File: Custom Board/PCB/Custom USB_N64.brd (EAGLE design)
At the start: 86 x 38.1 mm, 25 parts, among them J1 N64_Data, J2 N64_GND, U1 STM32F446RET6

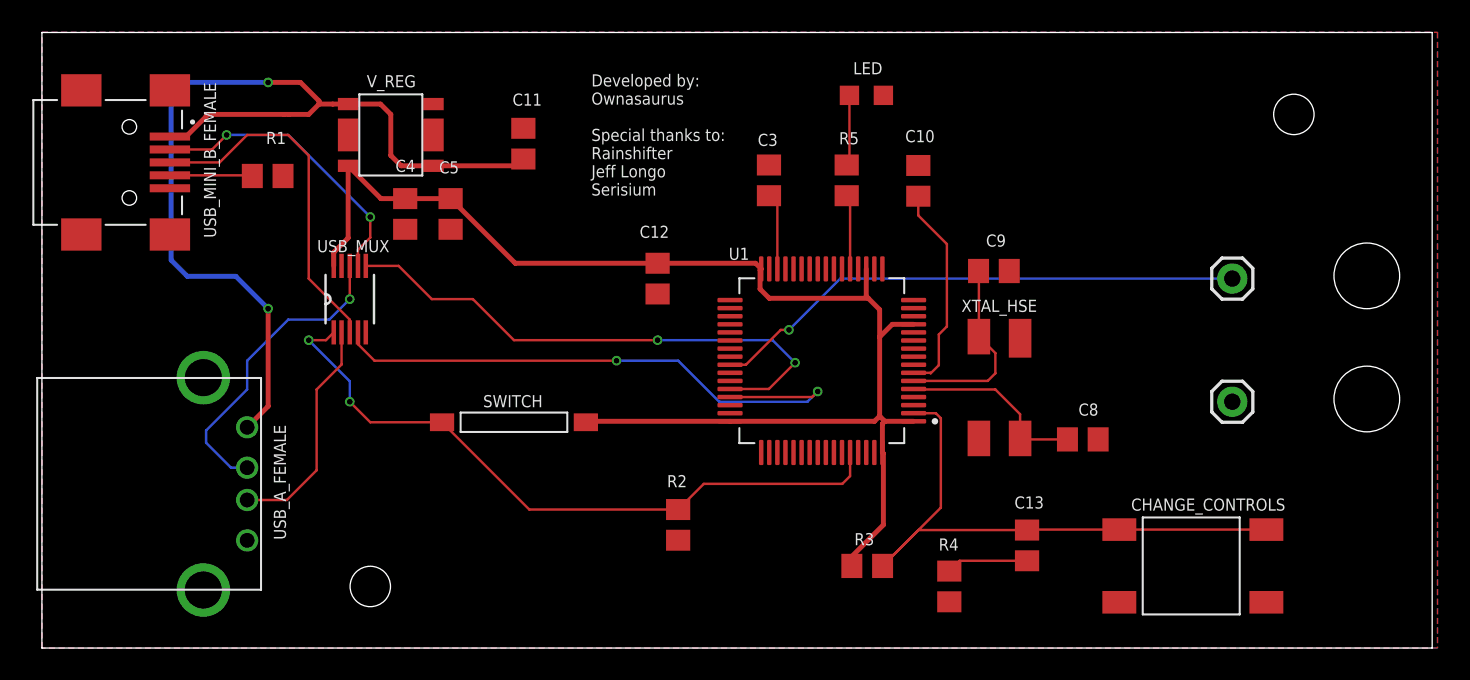
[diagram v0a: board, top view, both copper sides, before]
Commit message: fixed faulty V_REG foorprint and N64 silkscreen
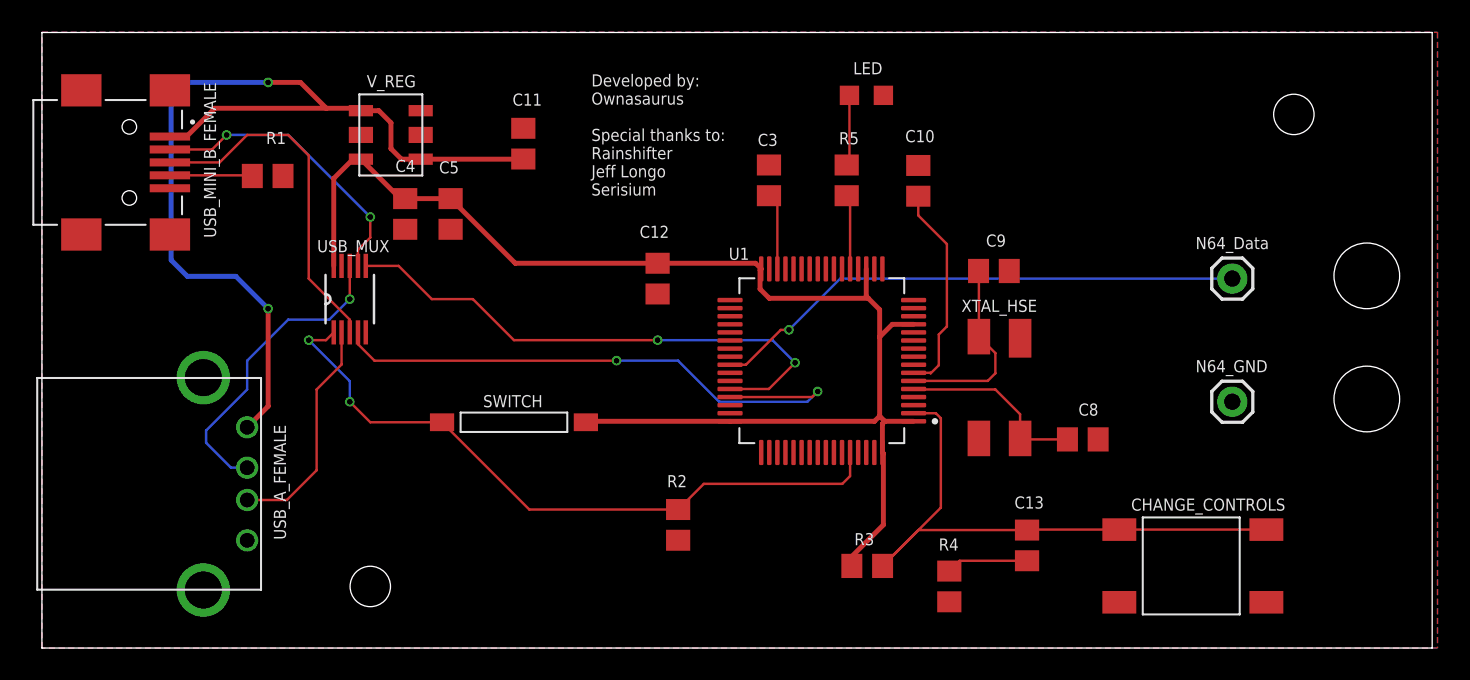
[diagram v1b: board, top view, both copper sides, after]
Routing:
- net +5V: track 61.3 -> 60.6 mm
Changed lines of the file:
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@@
 <drawing>
 <settings>
-<setting alwaysvectorfont="yes"/>
+<setting alwaysvectorfont="no"/>
 <setting verticaltext="up"/>
 </settings>
@@
 </element>
 <element name="J1" library="SparkFun-Connectors" package="1X01" value="N64_Data" x="73.66" y="22.86" smashed="yes">
-<attribute name="VALUE" x="71.39" y="24.685" size="0.75" layer="27" font="vector" ratio="15"/>
+<attribute name="VALUE" x="71.39" y="24.685" size="0.75" layer="25" font="vector" ratio="15"/>
 </element>
 <element name="J2" library="SparkFun-Connectors" package="1X01" value="N64_GND" x="73.66" y="15.24" smashed="yes">
-<attribute name="VALUE" x="71.39" y="17.065" size="0.75" layer="27" font="vector" ratio="15"/>
+<attribute name="VALUE" x="71.39" y="17.065" size="0.75" layer="25" font="vector" ratio="15"/>
 </element>
 <element name="C11" library="eagle-ltspice" library_urn="urn:adsk.eagle:library:217" package="C0805" package3d_urn="urn:adsk.eagle:package:13265/1" value="100nF" x="29.79" y="31.21" smashed="yes" rot="R270">
@@
 <wire x1="38.1" y1="23.81" x2="44.16" y2="23.81" width="0.3048" layer="1"/>
 <wire x1="44.51" y1="23.46" x2="44.16" y2="23.81" width="0.3048" layer="1"/>
-<wire x1="18.95" y1="29.84" x2="18.95" y2="25.37545" width="0.3048" layer="1"/>
 <wire x1="44.4382" y1="22.21375" x2="44.4382" y2="23.3882" width="0.3048" layer="1"/>
 <wire x1="53.94" y1="20.03" x2="52.62195" y2="20.03" width="0.3048" layer="1"/>
@@
 <wire x1="51.01" y1="21.76895" x2="51.01" y2="23.46" width="0.3048" layer="1"/>
 <wire x1="44.4382" y1="23.3882" x2="44.51" y2="23.46" width="0.3048" layer="1"/>
-<wire x1="18.95" y1="25.37545" x2="18.0594" y2="24.48485" width="0.3048" layer="1"/>
-<wire x1="18.0594" y1="24.48485" x2="18.0594" y2="23.6474" width="0.3048" layer="1"/>
 <wire x1="51.8392" y1="20.93975" x2="51.8392" y2="19.24725" width="0.3048" layer="1"/>
 <wire x1="51.8392" y1="14.351" x2="51.8392" y2="19.24725" width="0.3048" layer="1"/>
@@
 <wire x1="52.01" y1="12.1" x2="52.01" y2="13.8798" width="0.3048" layer="1"/>
 <wire x1="52.01" y1="13.8798" x2="52.1602" y2="14.03" width="0.3048" layer="1"/>
-<wire x1="18.95" y1="29.84" x2="20.98" y2="27.81" width="0.3048" layer="1"/>
-<wire x1="20.98" y1="27.81" x2="22.48" y2="27.81" width="0.3048" layer="1"/>
 <wire x1="22.48" y1="27.81" x2="25.29" y2="27.81" width="0.3048" layer="1"/>
 <wire x1="25.29" y1="27.81" x2="29.29" y2="23.81" width="0.3048" layer="1"/>
 <wire x1="29.29" y1="23.81" x2="38.1" y2="23.81" width="0.3048" layer="1"/>
+<wire x1="18.0594" y1="23.6474" x2="18.0594" y2="29.0594" width="0.3048" layer="1"/>
+<wire x1="19.25" y1="30.25" x2="19.74" y2="30.25" width="0.3048" layer="1"/>
+<wire x1="18.0594" y1="29.0594" x2="19.25" y2="30.25" width="0.3048" layer="1"/>
+<wire x1="19.74" y1="30.25" x2="22.18" y2="27.81" width="0.3048" layer="1"/>
+<wire x1="22.18" y1="27.81" x2="22.48" y2="27.81" width="0.3048" layer="1"/>
 </signal>
 <signal name="N$5">
@@
 <contactref element="V_REG" pad="EN"/>
 <contactref element="USB_MINI_B_FEMALE" pad="1"/>
-<wire x1="8.92" y1="31.65" x2="10.135" y2="32.865" width="0.3048" layer="1"/>
-<wire x1="10.29" y1="33.02" x2="10.135" y2="32.865" width="0.3048" layer="1"/>
-<wire x1="17.15" y1="33.66" x2="16.51" y2="33.02" width="0.3048" layer="1"/>
-<wire x1="17.15" y1="33.66" x2="18" y2="33.66" width="0.3048" layer="1"/>
-<wire x1="18" y1="33.66" x2="18.95" y2="33.66" width="0.3048" layer="1"/>
-<wire x1="18.95" y1="33.66" x2="20.95" y2="33.66" width="0.3048" layer="1"/>
-<wire x1="20.95" y1="33.66" x2="21.59" y2="33.02" width="0.3048" layer="1"/>
-<wire x1="21.59" y1="33.02" x2="21.59" y2="30.48" width="0.3048" layer="1"/>
-<wire x1="21.59" y1="30.48" x2="22.23" y2="29.84" width="0.3048" layer="1"/>
-<wire x1="22.23" y1="29.84" x2="24.23" y2="29.84" width="0.3048" layer="1"/>
 <contactref element="USB_A_FEMALE" pad="+5V"/>
 <wire x1="12.7" y1="13.66" x2="14" y2="14.96" width="0.3048" layer="1"/>
@@
 <wire x1="9" y1="35" x2="8" y2="34" width="0.3048" layer="16"/>
 <wire x1="8" y1="34" x2="8" y2="24" width="0.3048" layer="16"/>
-<wire x1="7.92" y1="31.65" x2="8.92" y2="31.65" width="0.3048" layer="1"/>
 <wire x1="8" y1="24" x2="9" y2="23" width="0.3048" layer="16"/>
 <wire x1="9" y1="23" x2="12" y2="23" width="0.3048" layer="16"/>
 <wire x1="12" y1="23" x2="14" y2="21" width="0.3048" layer="16"/>
-<wire x1="16.51" y1="33.02" x2="15.3" y2="33.02" width="0.3048" layer="1"/>
-<wire x1="15.3" y1="33.02" x2="15" y2="33.02" width="0.3048" layer="1"/>
-<wire x1="15" y1="33.02" x2="10.29" y2="33.02" width="0.3048" layer="1"/>
 <wire x1="14" y1="35" x2="16" y2="35" width="0.3048" layer="1"/>
-<wire x1="16" y1="35" x2="17.15" y2="33.85" width="0.3048" layer="1"/>
-<wire x1="17.15" y1="33.85" x2="17.15" y2="33.66" width="0.3048" layer="1"/>
-<wire x1="29.79" y1="30.26" x2="29.37" y2="29.84" width="0.3048" layer="1"/>
-<wire x1="29.37" y1="29.84" x2="24.23" y2="29.84" width="0.3048" layer="1"/>
+<wire x1="19.74" y1="33.25" x2="20.85" y2="33.25" width="0.3048" layer="1"/>
+<wire x1="20.85" y1="33.25" x2="21.6" y2="32.5" width="0.3048" layer="1"/>
+<wire x1="21.6" y1="32.5" x2="21.6" y2="30.9" width="0.3048" layer="1"/>
+<wire x1="22.25" y1="30.25" x2="23.44" y2="30.25" width="0.3048" layer="1"/>
+<wire x1="21.6" y1="30.9" x2="22.25" y2="30.25" width="0.3048" layer="1"/>
+<wire x1="23.44" y1="30.25" x2="29.78" y2="30.25" width="0.3048" layer="1"/>
+<wire x1="29.78" y1="30.25" x2="29.79" y2="30.26" width="0.3048" layer="1"/>
+<wire x1="7.92" y1="31.65" x2="8.95" y2="31.65" width="0.3048" layer="1"/>
+<wire x1="8.95" y1="31.65" x2="10.7" y2="33.4" width="0.3048" layer="1"/>
+<wire x1="10.7" y1="33.4" x2="17.6" y2="33.4" width="0.3048" layer="1"/>
+<wire x1="17.6" y1="33.4" x2="19.59" y2="33.4" width="0.3048" layer="1"/>
+<wire x1="19.59" y1="33.4" x2="19.74" y2="33.25" width="0.3048" layer="1"/>
+<wire x1="16" y1="35" x2="17.6" y2="33.4" width="0.3048" layer="1"/>
 </signal>
 <signal name="N$15">
